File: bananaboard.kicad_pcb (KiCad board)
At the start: 2 copper layers, 87 parts, among them J1 prog_pins, J2 Conn_01x01, J3 Conn_01x01, J5 Conn_01x01, J7 Conn_01x01, J8 Conn-Battery, U1 cargador-USB, U2 core51822, U3 LM1117-3.3

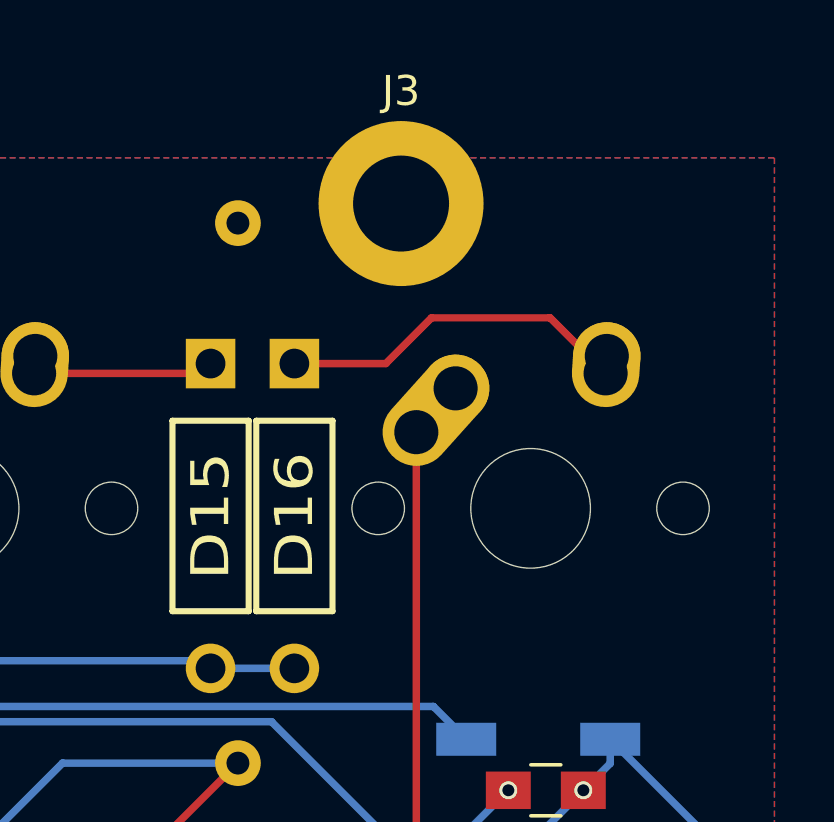
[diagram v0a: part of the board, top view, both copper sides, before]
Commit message: Moved screw hole
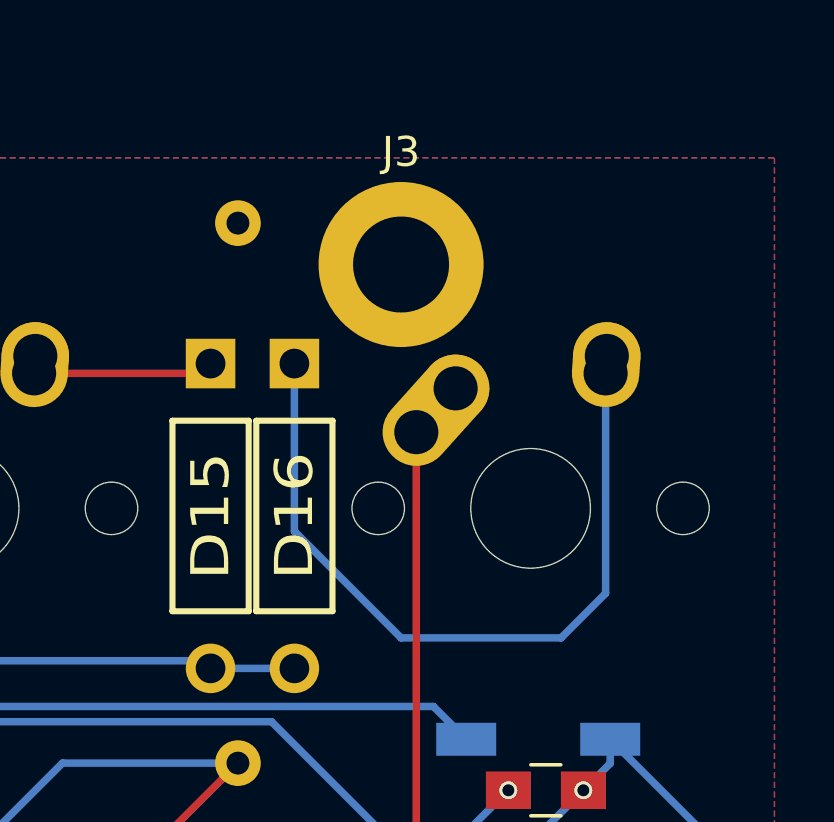
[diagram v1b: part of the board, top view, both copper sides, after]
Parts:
- moved J3 2.03 mm to (112.5, 13.5)
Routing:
- net Net-(D16-Pad2): track 11.8 -> 25.4 mm
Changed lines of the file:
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@@
     (thickness 1.6)
     (drawings 0)
-    (tracks 531)
+    (tracks 532)
     (zones 0)
     (modules 87)
@@
   )
   (module Mounting_Holes:MountingHole_3.2mm_M3_ISO14580_Pad (layer F.Cu)
-    (at 112.522 11.43)
+    (at 112.522 13.462)
     (descr "Mounting Hole 3.2mm, M3, ISO14580")
     (tags "mounting hole 3.2mm m3 iso14580")
@@
   (segment (start 100.29 17.09) (end 105.846 17.09) (width 0.25) (layer F.Cu) (net 7))
   (segment (start 105.846 17.09) (end 106.172 16.764) (width 0.25) (layer F.Cu) (net 7))
-  (segment (start 108.966 16.764) (end 112.014 16.764) (width 0.25) (layer F.Cu) (net 8))
-  (segment (start 117.49 15.24) (end 119.34 17.09) (width 0.25) (layer F.Cu) (net 8))
-  (segment (start 113.538 15.24) (end 117.49 15.24) (width 0.25) (layer F.Cu) (net 8))
-  (segment (start 112.014 16.764) (end 113.538 15.24) (width 0.25) (layer F.Cu) (net 8))
+  (segment (start 108.966 16.764) (end 108.966 22.352) (width 0.25) (layer B.Cu) (net 8))
+  (segment (start 119.34 24.424) (end 119.34 17.09) (width 0.25) (layer B.Cu) (net 8))
+  (segment (start 117.856 25.908) (end 119.34 24.424) (width 0.25) (layer B.Cu) (net 8))
+  (segment (start 112.522 25.908) (end 117.856 25.908) (width 0.25) (layer B.Cu) (net 8))
+  (segment (start 108.966 22.352) (end 112.522 25.908) (width 0.25) (layer B.Cu) (net 8))
   (segment (start 24.09 36.14) (end 29.392 36.14) (width 0.25) (layer F.Cu) (net 9))
   (segment (start 29.392 36.14) (end 29.972 35.56) (width 0.25) (layer F.Cu) (net 9))

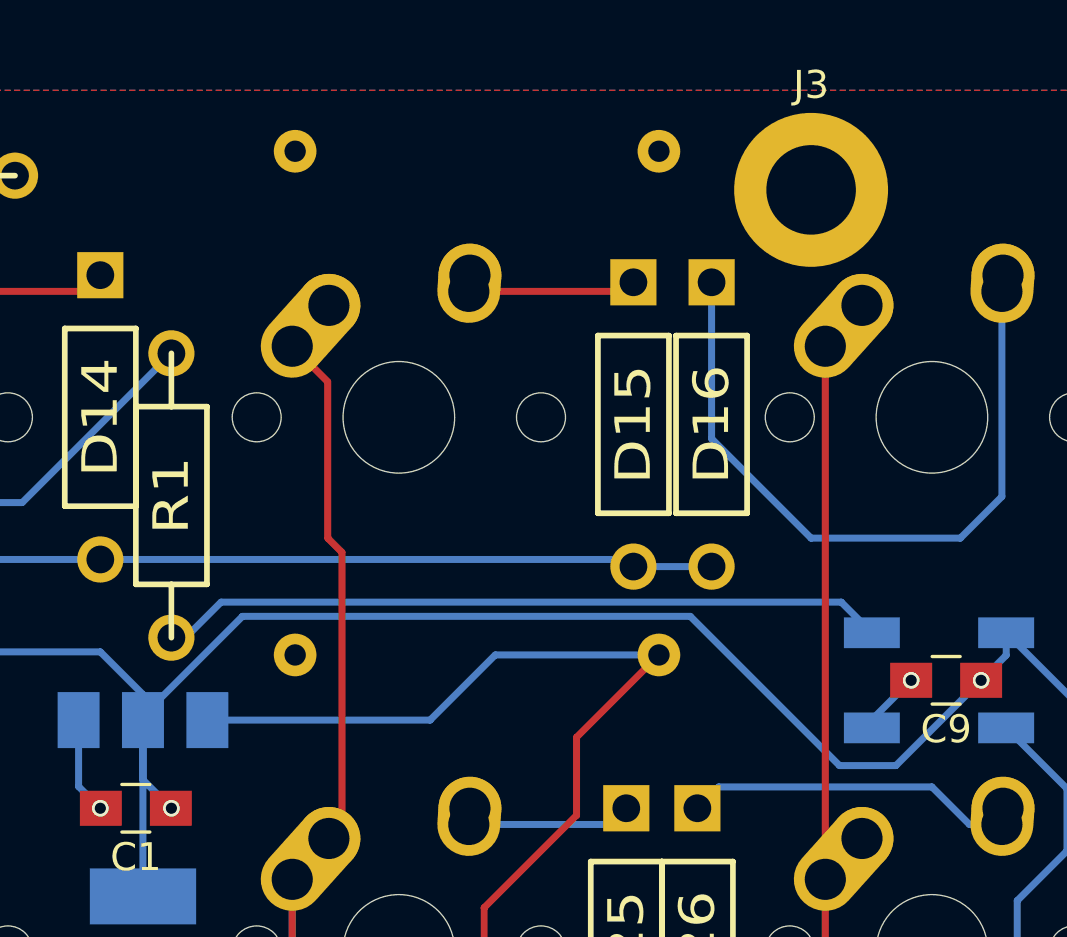
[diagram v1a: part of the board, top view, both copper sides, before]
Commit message: added images folder, moved diode and mounting hole
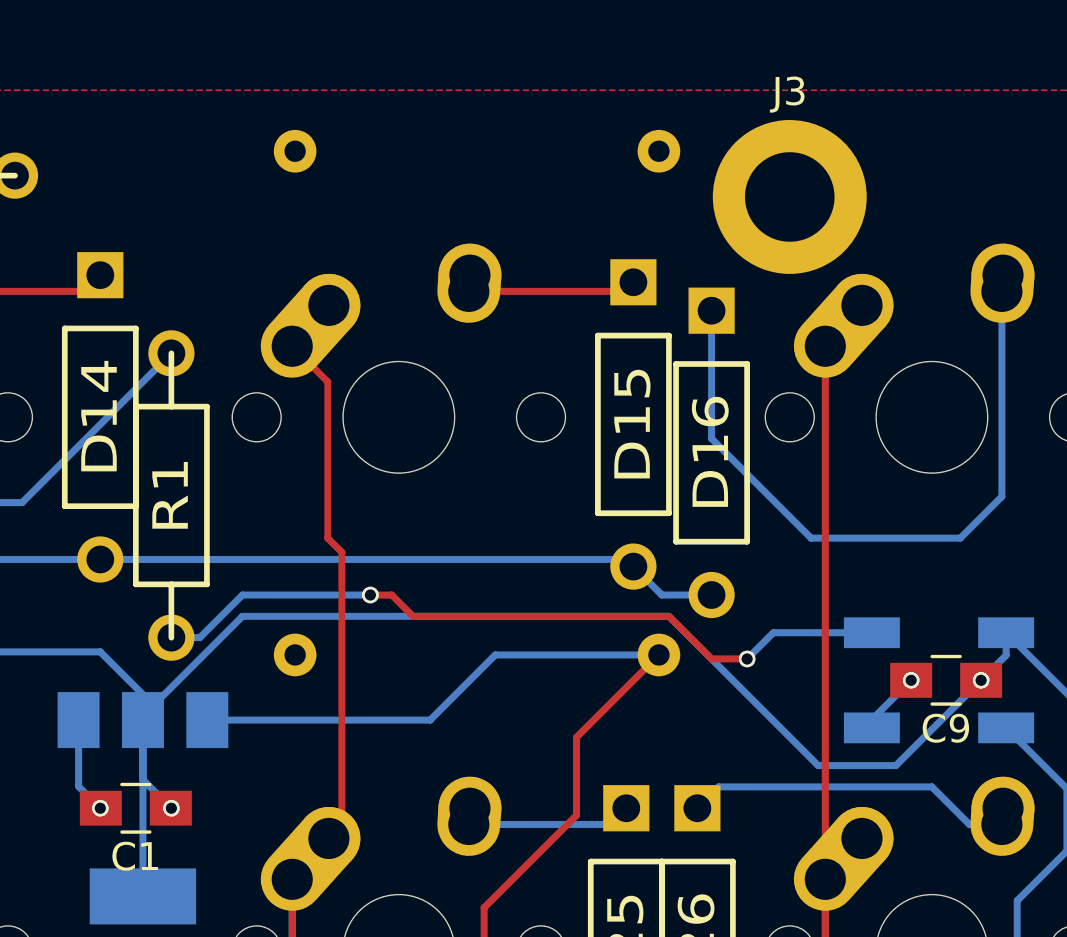
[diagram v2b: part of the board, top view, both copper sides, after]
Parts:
- moved D16 1.02 mm to (109.0, 22.9)
- moved J3 0.80 mm to (111.8, 13.7)
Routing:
- net Net-(D16-Pad2): track 25.4 -> 24.4 mm
- net Net-(LED1-Pad4): track 26.0 -> 27.0 mm, vias 0 -> 2
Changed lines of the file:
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@@
   (general
     (links 204)
-    (no_connects 0)
+    (no_connects 18)
     (area 11.789999 6.705 126.640001 88.540001)
     (thickness 1.6)
     (drawings 0)
-    (tracks 532)
+    (tracks 541)
     (zones 0)
     (modules 87)
@@
     (38 B.Mask user)
     (39 F.Mask user)
-    (40 Dwgs.User user hide)
+    (40 Dwgs.User user)
     (41 Cmts.User user)
     (42 Eco1.User user)
@@
   )
   (module footprints:DIODE (layer F.Cu)
-    (at 108.966 21.844 90)
+    (at 108.966 22.86 90)
     (fp_text reference D16 (at 0 0 90) (layer F.SilkS)
       (effects (font (size 1.27 1.524) (thickness 0.2032)))
@@
   )
   (module Mounting_Holes:MountingHole_3.2mm_M3_ISO14580_Pad (layer F.Cu)
-    (at 112.522 13.462)
+    (at 111.76 13.716)
     (descr "Mounting Hole 3.2mm, M3, ISO14580")
     (tags "mounting hole 3.2mm m3 iso14580")
@@
   (segment (start 88.646 32.41) (end 88.646 32.258) (width 0.25) (layer B.Cu) (net 1))
   (segment (start 88.646 32.258) (end 92.202 28.702) (width 0.25) (layer B.Cu) (net 1))
-  (segment (start 92.202 28.702) (end 108.204 28.702) (width 0.25) (layer B.Cu) (net 1))
-  (segment (start 108.204 28.702) (end 113.538 34.036) (width 0.25) (layer B.Cu) (net 1))
-  (segment (start 113.538 34.036) (end 115.55 34.036) (width 0.25) (layer B.Cu) (net 1))
+  (segment (start 92.202 28.702) (end 107.442 28.702) (width 0.25) (layer B.Cu) (net 1))
+  (segment (start 107.442 28.702) (end 112.776 34.036) (width 0.25) (layer B.Cu) (net 1))
+  (segment (start 112.776 34.036) (end 115.55 34.036) (width 0.25) (layer B.Cu) (net 1))
   (segment (start 115.55 34.036) (end 118.598 30.988) (width 0.25) (layer B.Cu) (net 1))
   (via (at 118.598 30.988) (size 0.6) (drill 0.4) (layers F.Cu B.Cu) (net 1))
@@
   (segment (start 100.29 17.09) (end 105.846 17.09) (width 0.25) (layer F.Cu) (net 7))
   (segment (start 105.846 17.09) (end 106.172 16.764) (width 0.25) (layer F.Cu) (net 7))
-  (segment (start 108.966 16.764) (end 108.966 22.352) (width 0.25) (layer B.Cu) (net 8))
-  (segment (start 119.34 24.424) (end 119.34 17.09) (width 0.25) (layer B.Cu) (net 8))
-  (segment (start 117.856 25.908) (end 119.34 24.424) (width 0.25) (layer B.Cu) (net 8))
-  (segment (start 112.522 25.908) (end 117.856 25.908) (width 0.25) (layer B.Cu) (net 8))
+  (segment (start 108.966 17.78) (end 108.966 22.352) (width 0.25) (layer B.Cu) (net 8))
   (segment (start 108.966 22.352) (end 112.522 25.908) (width 0.25) (layer B.Cu) (net 8))
+  (segment (start 112.522 25.908) (end 117.856 25.908) (width 0.25) (layer B.Cu) (net 8))
+  (segment (start 117.856 25.908) (end 119.34 24.424) (width 0.25) (layer B.Cu) (net 8))
+  (segment (start 119.34 24.424) (end 119.34 17.09) (width 0.25) (layer B.Cu) (net 8))
   (segment (start 24.09 36.14) (end 29.392 36.14) (width 0.25) (layer F.Cu) (net 9))
   (segment (start 29.392 36.14) (end 29.972 35.56) (width 0.25) (layer F.Cu) (net 9))
@@
   (segment (start 119.888 42.672) (end 119.888 38.862) (width 0.25) (layer B.Cu) (net 27))
   (segment (start 114.694 47.866) (end 119.888 42.672) (width 0.25) (layer B.Cu) (net 27))
-  (segment (start 89.662 29.464) (end 90.17 29.464) (width 0.25) (layer B.Cu) (net 28))
-  (segment (start 113.6 28.194) (end 114.694 29.288) (width 0.25) (layer B.Cu) (net 28))
-  (segment (start 91.44 28.194) (end 113.6 28.194) (width 0.25) (layer B.Cu) (net 28))
-  (segment (start 90.17 29.464) (end 91.44 28.194) (width 0.25) (layer B.Cu) (net 28))
+  (segment (start 114.694 29.288) (end 111.174 29.288) (width 0.25) (layer B.Cu) (net 28) (status 400000))
+  (segment (start 90.678 29.464) (end 89.662 29.464) (width 0.25) (layer B.Cu) (net 28) (status 800000))
+  (segment (start 92.202 27.94) (end 90.678 29.464) (width 0.25) (layer B.Cu) (net 28))
+  (segment (start 96.774 27.94) (end 92.202 27.94) (width 0.25) (layer B.Cu) (net 28))
+  (via (at 96.774 27.94) (size 0.6) (drill 0.4) (layers F.Cu B.Cu) (net 28))
+  (segment (start 97.536 27.94) (end 96.774 27.94) (width 0.25) (layer F.Cu) (net 28))
+  (segment (start 98.298 28.702) (end 97.536 27.94) (width 0.25) (layer F.Cu) (net 28))
+  (segment (start 107.442 28.702) (end 98.298 28.702) (width 0.25) (layer F.Cu) (net 28))
+  (segment (start 108.966 30.226) (end 107.442 28.702) (width 0.25) (layer F.Cu) (net 28))
+  (segment (start 110.236 30.226) (end 108.966 30.226) (width 0.25) (layer F.Cu) (net 28))
+  (via (at 110.236 30.226) (size 0.6) (drill 0.4) (layers F.Cu B.Cu) (net 28))
+  (segment (start 111.174 29.288) (end 110.236 30.226) (width 0.25) (layer B.Cu) (net 28))
   (segment (start 114.694 67.388) (end 114.694 66.408) (width 0.25) (layer B.Cu) (net 29))
   (segment (start 122.428 54.926) (end 119.494 51.992) (width 0.25) (layer B.Cu) (net 29))
@@
   (segment (start 113.792 72.898) (end 117.384 72.898) (width 0.25) (layer B.Cu) (net 30))
   (segment (start 110.858 75.832) (end 113.792 72.898) (width 0.25) (layer B.Cu) (net 30))
+  (segment (start 108.966 27.94) (end 107.188 27.94) (width 0.25) (layer B.Cu) (net 31))
+  (segment (start 107.188 27.94) (end 106.172 26.924) (width 0.25) (layer B.Cu) (net 31))
   (segment (start 87.122 26.67) (end 105.918 26.67) (width 0.25) (layer B.Cu) (net 31))
   (segment (start 105.918 26.67) (end 106.172 26.924) (width 0.25) (layer B.Cu) (net 31))
-  (segment (start 106.172 26.924) (end 108.966 26.924) (width 0.25) (layer B.Cu) (net 31))
   (segment (start 60.706 25.571) (end 65.869 25.571) (width 0.25) (layer B.Cu) (net 31))
   (segment (start 73.914 26.67) (end 87.122 26.67) (width 0.25) (layer B.Cu) (net 31))
@@
     (connect_pads (clearance 0.508))
     (min_thickness 0.254)
-    (fill yes (arc_segments 16) (thermal_gap 0.508) (thermal_bridge_width 0.508))
+    (fill (arc_segments 16) (thermal_gap 0.508) (thermal_bridge_width 0.508))
     (polygon
       (pts
@@
     (connect_pads (clearance 0.508))
     (min_thickness 0.254)
-    (fill yes (arc_segments 16) (thermal_gap 0.508) (thermal_bridge_width 0.508))
+    (fill (arc_segments 16) (thermal_gap 0.508) (thermal_bridge_width 0.508))
     (polygon
       (pts
